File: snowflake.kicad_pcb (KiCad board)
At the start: 6 copper layers, 127.8 x 134.4 mm, 90 parts, among them J1 2.1mm Jack, J2 ARM-JTAG-SWD-10, J3 Debug, J4 USB, U1 TPSM84424, U2 TPS62291, U3 LP5036, U4 LP5036, U5 LP5036, U6 STM32F413CHUx, U7 M95512, U8 TPD3S014, Y1 32.768K, Y2 16Mhz

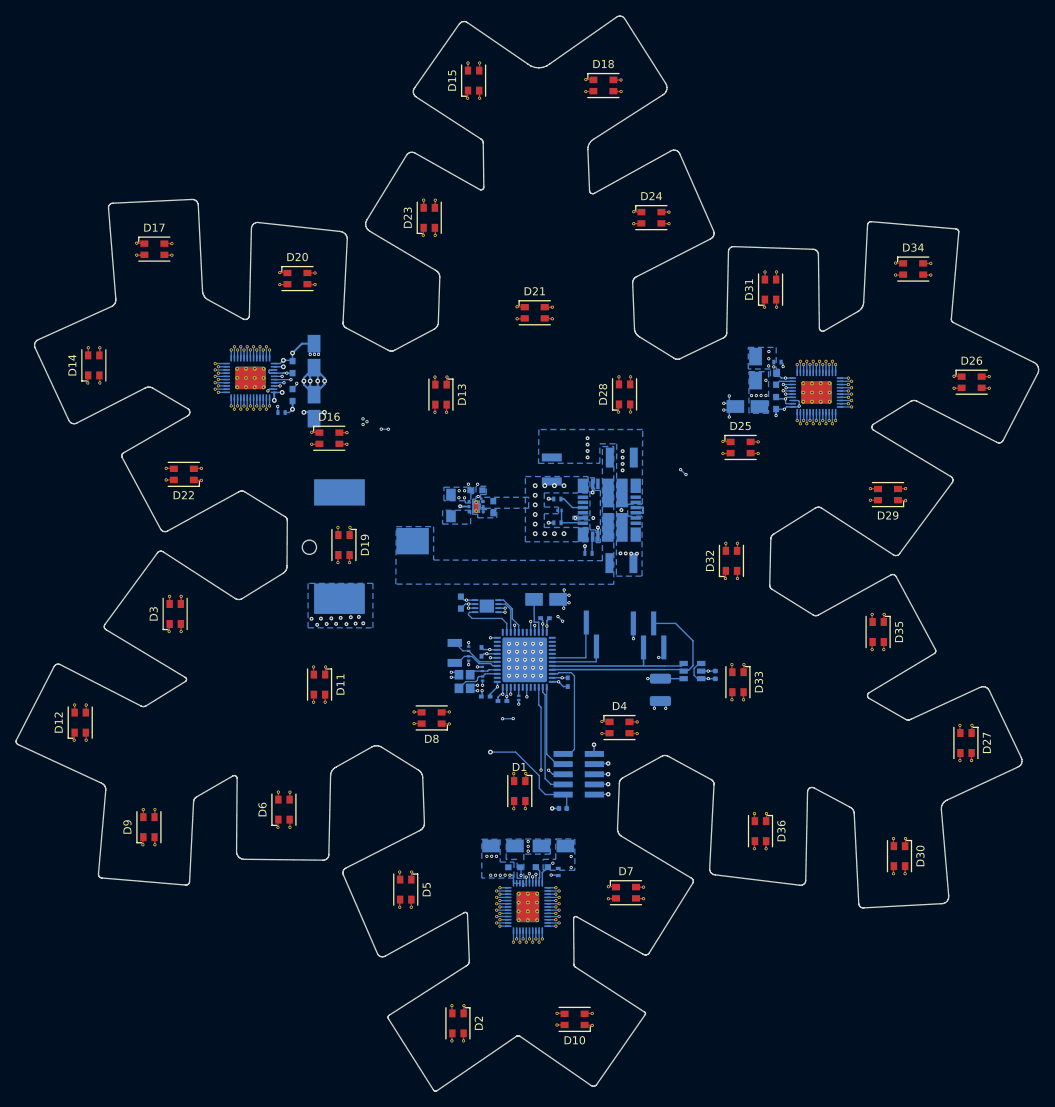
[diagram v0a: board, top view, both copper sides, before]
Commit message: Merged usb and debug to single 1.27mm header.
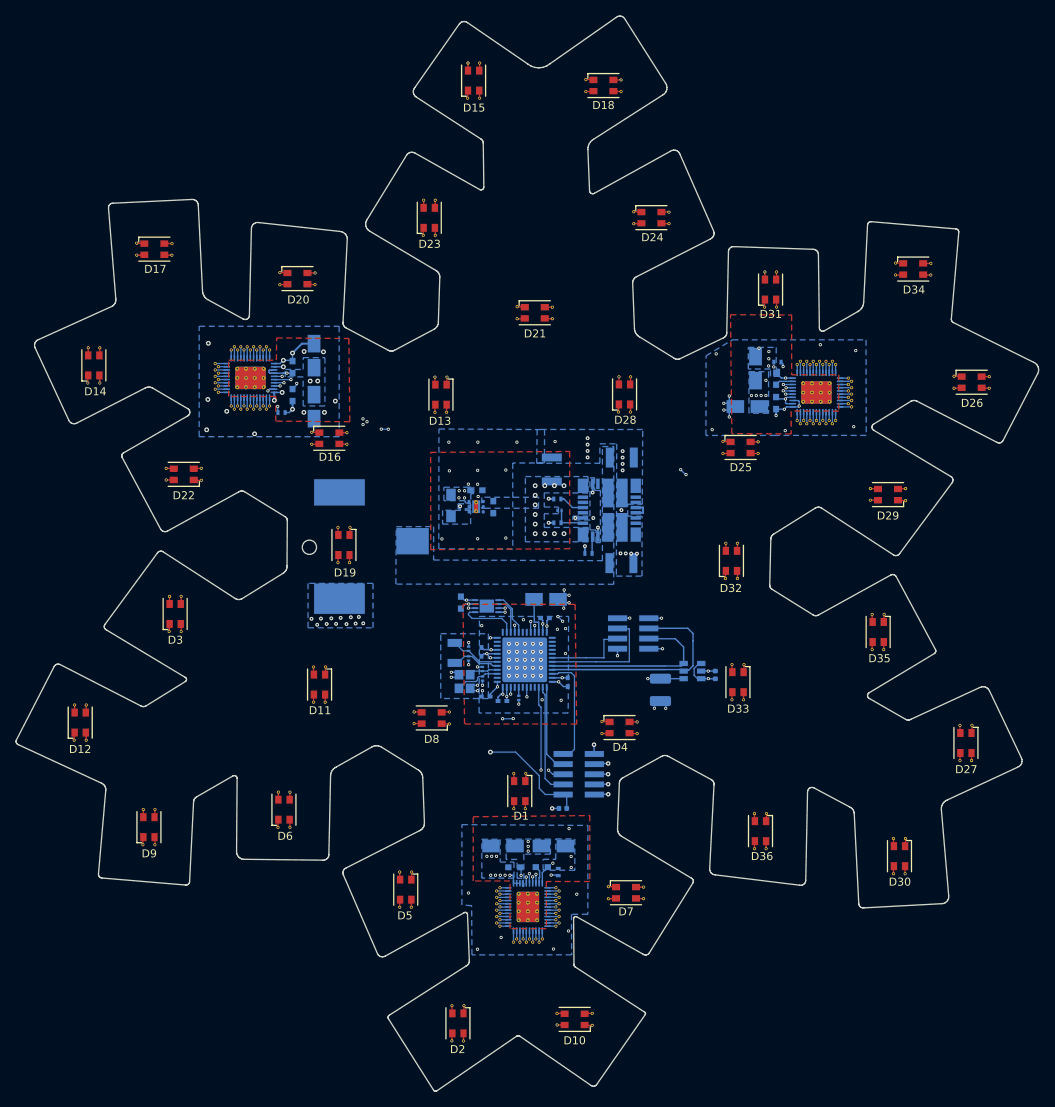
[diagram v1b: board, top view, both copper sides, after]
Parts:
- removed J4: USB, Connector_PinHeader_1.27mm:PinHeader_1x04_P1.27mm_Vertical_SMD_Pin1Left
- J3: value Debug -> 2x4-1.27mm-0.05in; footprint Pin_Headers:Pin_Header_Straight_1x02_Pitch1.27mm_SMD_Pin1Left -> snowflake:PinHeader_2x04_P1.27mm_Vertical_SMD_CCW
- moved J3 5.22 mm to (149.9, 111.7), turned to 180 degrees
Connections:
- J3 pad 1: /MCU/DBG_RX -> /MCU/VBUS
- J3 pad 2: /MCU/DBG_TX -> /MCU/USB-D+
- U3 pad 47: Net-(U3-Pad47) -> GND
- U4 pad 47: Net-(U4-Pad47) -> GND
- U5 pad 47: Net-(U5-Pad47) -> GND
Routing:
- net +5V: track 32.3 -> 17.4 mm, vias 29 -> 27
- net +3V3: track 90.0 -> 103.4 mm, vias 13 -> 14
- net /MCU/DBG_RX: track 7.50 -> 15.3 mm
- net /MCU/VBUS: track 8.29 -> 14.4 mm
- net GND: track 70.6 -> 65.8 mm, vias 115 -> 152
- net /MCU/USB-D-: track 18.9 -> 23.5 mm
- net /MCU/DBG_TX: track 8.62 -> 10.6 mm
- net /MCU/USB-D+: track 27.0 -> 27.9 mm
- added copper zone on F.Cu, net GND
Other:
- board text added: "+3V3"
